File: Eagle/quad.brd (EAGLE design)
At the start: 72 x 46 mm, 12 parts

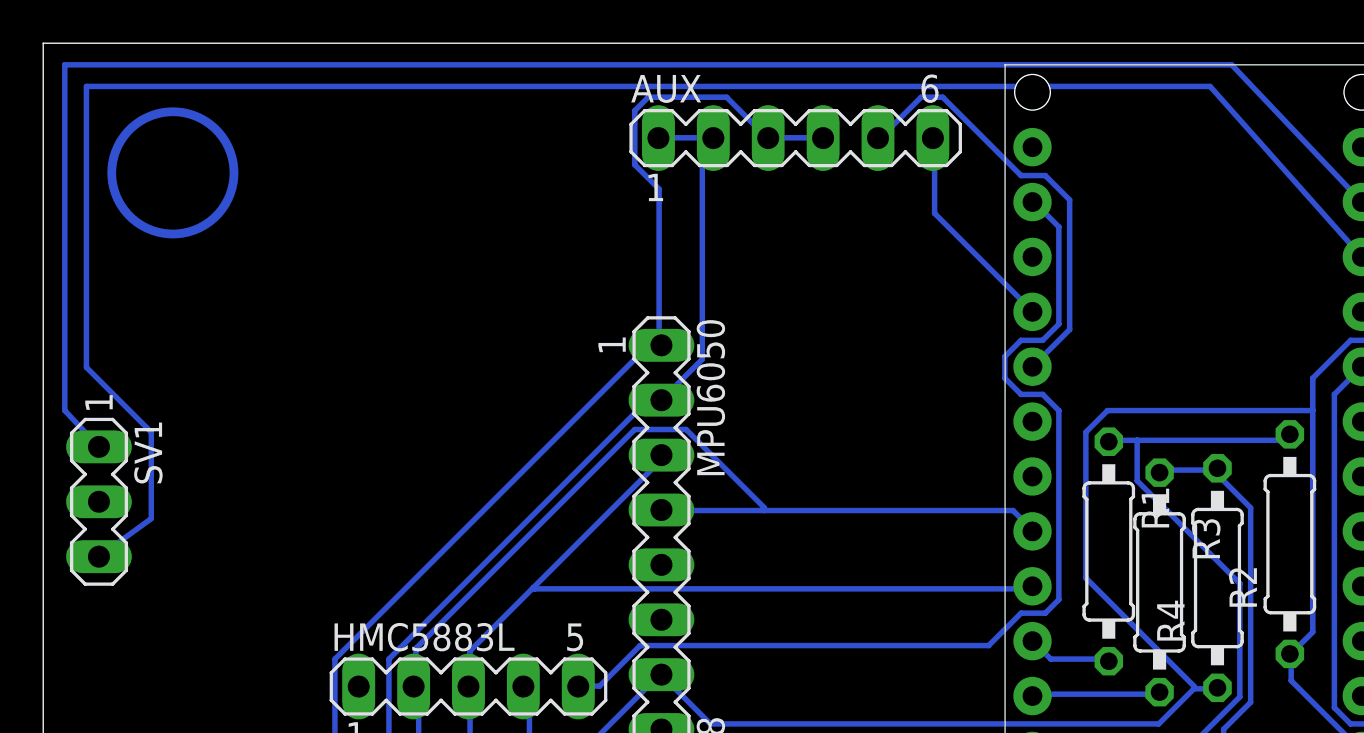
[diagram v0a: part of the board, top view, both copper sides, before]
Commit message: Added acrobtic mode. Not tested yet.
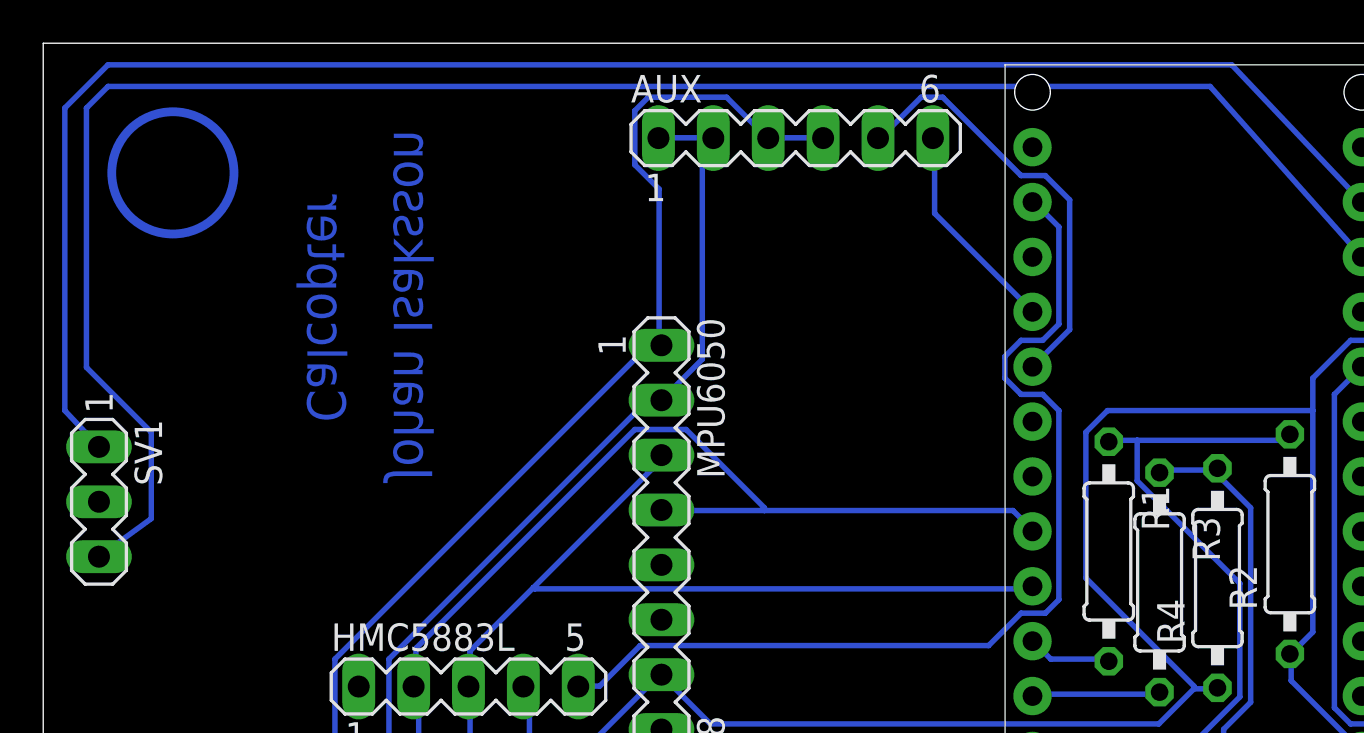
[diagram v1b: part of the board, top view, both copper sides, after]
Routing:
- net N$4: track 81.1 -> 79.9 mm
- net N$3: track 86.8 -> 86.2 mm
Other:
- board text added: "Calcopter"
- board text added: "Johan Isaksson"
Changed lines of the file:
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@@
 <?xml version="1.0" encoding="utf-8"?>
 <!DOCTYPE eagle SYSTEM "eagle.dtd">
-<eagle version="7.4.0">
+<eagle version="7.5.0">
 <drawing>
 <settings>
@@
 <layer number="17" name="Pads" color="2" fill="1" visible="yes" active="yes"/>
 <layer number="18" name="Vias" color="2" fill="1" visible="yes" active="yes"/>
-<layer number="19" name="Unrouted" color="6" fill="1" visible="yes" active="yes"/>
-<layer number="20" name="Dimension" color="15" fill="1" visible="yes" active="yes"/>
-<layer number="21" name="tPlace" color="7" fill="1" visible="yes" active="yes"/>
-<layer number="22" name="bPlace" color="7" fill="1" visible="yes" active="yes"/>
-<layer number="23" name="tOrigins" color="15" fill="1" visible="yes" active="yes"/>
-<layer number="24" name="bOrigins" color="15" fill="1" visible="yes" active="yes"/>
-<layer number="25" name="tNames" color="7" fill="1" visible="yes" active="yes"/>
-<layer number="26" name="bNames" color="7" fill="1" visible="yes" active="yes"/>
-<layer number="27" name="tValues" color="7" fill="1" visible="yes" active="yes"/>
-<layer number="28" name="bValues" color="7" fill="1" visible="yes" active="yes"/>
+<layer number="19" name="Unrouted" color="6" fill="1" visible="no" active="yes"/>
+<layer number="20" name="Dimension" color="15" fill="1" visible="no" active="yes"/>
+<layer number="21" name="tPlace" color="7" fill="1" visible="no" active="yes"/>
+<layer number="22" name="bPlace" color="7" fill="1" visible="no" active="yes"/>
+<layer number="23" name="tOrigins" color="15" fill="1" visible="no" active="yes"/>
+<layer number="24" name="bOrigins" color="15" fill="1" visible="no" active="yes"/>
+<layer number="25" name="tNames" color="7" fill="1" visible="no" active="yes"/>
+<layer number="26" name="bNames" color="7" fill="1" visible="no" active="yes"/>
+<layer number="27" name="tValues" color="7" fill="1" visible="no" active="yes"/>
+<layer number="28" name="bValues" color="7" fill="1" visible="no" active="yes"/>
 <layer number="29" name="tStop" color="7" fill="3" visible="no" active="yes"/>
 <layer number="30" name="bStop" color="7" fill="6" visible="no" active="yes"/>
@@
 <layer number="37" name="tTest" color="7" fill="1" visible="no" active="yes"/>
 <layer number="38" name="bTest" color="7" fill="1" visible="no" active="yes"/>
-<layer number="39" name="tKeepout" color="4" fill="11" visible="yes" active="yes"/>
-<layer number="40" name="bKeepout" color="1" fill="11" visible="yes" active="yes"/>
-<layer number="41" name="tRestrict" color="4" fill="10" visible="yes" active="yes"/>
-<layer number="42" name="bRestrict" color="1" fill="10" visible="yes" active="yes"/>
-<layer number="43" name="vRestrict" color="2" fill="10" visible="yes" active="yes"/>
+<layer number="39" name="tKeepout" color="4" fill="11" visible="no" active="yes"/>
+<layer number="40" name="bKeepout" color="1" fill="11" visible="no" active="yes"/>
+<layer number="41" name="tRestrict" color="4" fill="10" visible="no" active="yes"/>
+<layer number="42" name="bRestrict" color="1" fill="10" visible="no" active="yes"/>
+<layer number="43" name="vRestrict" color="2" fill="10" visible="no" active="yes"/>
 <layer number="44" name="Drills" color="7" fill="1" visible="no" active="yes"/>
 <layer number="45" name="Holes" color="7" fill="1" visible="no" active="yes"/>
 <layer number="46" name="Milling" color="3" fill="1" visible="no" active="yes"/>
 <layer number="47" name="Measures" color="7" fill="1" visible="no" active="yes"/>
-<layer number="48" name="Document" color="7" fill="1" visible="yes" active="yes"/>
-<layer number="49" name="Reference" color="7" fill="1" visible="yes" active="yes"/>
-<layer number="51" name="tDocu" color="7" fill="1" visible="yes" active="yes"/>
-<layer number="52" name="bDocu" color="7" fill="1" visible="yes" active="yes"/>
+<layer number="48" name="Document" color="7" fill="1" visible="no" active="yes"/>
+<layer number="49" name="Reference" color="7" fill="1" visible="no" active="yes"/>
+<layer number="51" name="tDocu" color="7" fill="1" visible="no" active="yes"/>
+<layer number="52" name="bDocu" color="7" fill="1" visible="no" active="yes"/>
 <layer number="90" name="Modules" color="5" fill="1" visible="no" active="no"/>
 <layer number="91" name="Nets" color="2" fill="1" visible="no" active="no"/>
@@
 <circle x="6" y="6" radius="2.828425" width="0.4064" layer="16"/>
 <circle x="66" y="6" radius="2.828425" width="0.4064" layer="16"/>
+<text x="18" y="42" size="1.778" layer="16" rot="MR270">Johan Isaksson</text>
+<text x="14" y="39" size="1.778" layer="16" rot="MR270">Calcopter</text>
 </plain>
 <attributes>
@@
 <wire x1="5" y1="24" x2="5" y2="28" width="0.254" layer="16"/>
 <wire x1="5" y1="28" x2="2" y2="31" width="0.254" layer="16"/>
-<wire x1="2" y1="31" x2="2" y2="44" width="0.254" layer="16"/>
-<wire x1="2" y1="44" x2="54" y2="44" width="0.254" layer="16"/>
+<wire x1="2" y1="44" x2="54" y2="44" width="0" layer="19" extent="1-16"/>
 <wire x1="54" y1="44" x2="61.02" y2="36.11" width="0.254" layer="16"/>
+<wire x1="2" y1="31" x2="2" y2="43" width="0.254" layer="16"/>
+<wire x1="2" y1="43" x2="3" y2="44" width="0.254" layer="16"/>
+<wire x1="3" y1="44" x2="54" y2="44" width="0.254" layer="16"/>
 </signal>
 <signal name="N$5">
@@
 <contactref element="SV1" pad="1"/>
 <wire x1="61.02" y1="38.65" x2="55" y2="45" width="0.254" layer="16"/>
-<wire x1="55" y1="45" x2="1" y2="45" width="0.254" layer="16"/>
-<wire x1="1" y1="45" x2="1" y2="29" width="0.254" layer="16"/>
 <wire x1="1" y1="29" x2="2.58" y2="27.32" width="0.254" layer="16"/>
+<wire x1="55" y1="45" x2="3" y2="45" width="0.254" layer="16"/>
+<wire x1="3" y1="45" x2="1" y2="43" width="0.254" layer="16"/>
+<wire x1="1" y1="43" x2="1" y2="29" width="0.254" layer="16"/>
 </signal>
 </signals>

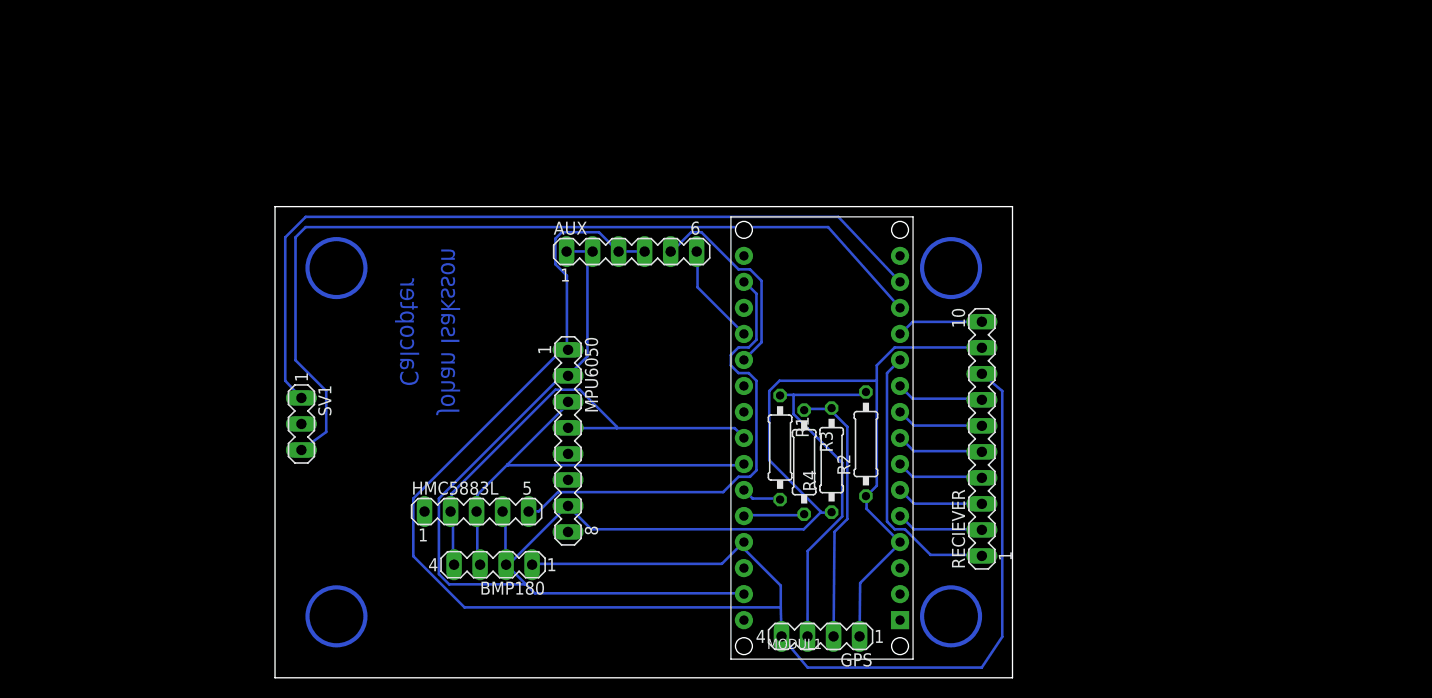
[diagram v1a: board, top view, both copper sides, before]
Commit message: Worked on board for the large quad.
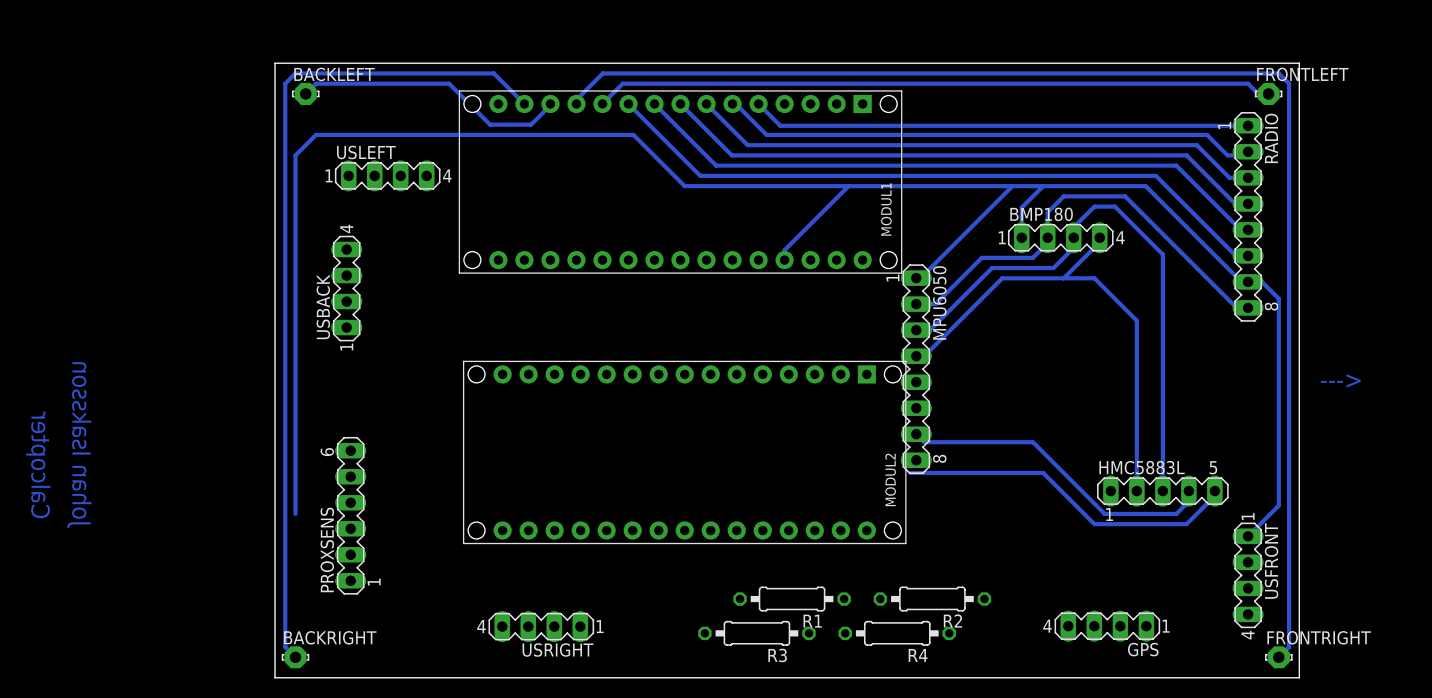
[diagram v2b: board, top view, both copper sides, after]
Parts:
- removed AUX: (no value), con-lstb:MA06-1
- removed RECIEVER: (no value), con-lstb:MA10-1
- removed SV1: (no value), con-lstb:MA03-1
- added BACKLEFT, BACKRIGHT, FRONTLEFT, FRONTRIGHT: LSP11, solpad:LSP11
- added MODUL2: ARDUINO_NANO2, arduino:ARDUINO_NANO2
- added PROXSENS: (no value), con-lstb:MA06-1
- added RADIO: (no value), con-lstb:MA08-1
- added USBACK, USFRONT, USLEFT, USRIGHT: (no value), con-lstb:MA04-1
- moved HMC5883L 67.0 mm to (86.7, 18.2)
- moved BMP180 64.0 mm to (76.7, 43.0), turned to 0 degrees
- moved MPU6050 34.7 mm to (62.6, 30.1)
- moved MODUL1 28.6 mm to (39.6, 48.4), turned to 270 degrees
- moved GPS 28.0 mm to (81.3, 5.04)
- moved R4 18.1 mm to (60.8, 4.34), turned to 180 degrees
- moved R3 17.3 mm to (47.0, 4.34), turned to 180 degrees
- moved R2 16.5 mm to (64.2, 7.69), turned to 180 degrees
- moved R1 14.8 mm to (50.5, 7.69), turned to 180 degrees
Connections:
- new net N$22: MODUL2.J1.7, USFRONT.2
- new net N$23: MODUL2.J1.8, USFRONT.3
- new net N$24: MODUL2.J1.5, USLEFT.2
- new net N$25: MODUL2.J1.6, USLEFT.3
- new net N$26: MODUL2.J1.9, USRIGHT.2
- new net N$27: MODUL2.J1.10, USRIGHT.3
- new net N$29: MODUL2.J1.12, USBACK.3
- new net N$30: MODUL2.J1.11, USBACK.2
- net AREF: now also MODUL2.J2.13
- net N$1: now also FRONTLEFT.MP; no longer RECIEVER.1
- net N$10: now also MODUL2.J2.11, PROXSENS.5; no longer AUX.6, MODUL1.J2.12
- net N$11: now also RADIO.4; no longer RECIEVER.5
- net N$12: now also RADIO.5; no longer RECIEVER.6
- net N$13: now also RADIO.6; no longer RECIEVER.7
- net N$14: now also MODUL2.J2.14
- net N$15: now also MODUL2.J2.5; no longer MODUL1.J2.5
- net N$16: now also MODUL2.J2.7
- net N$17: now also MODUL2.J2.8
- net N$18: now also MODUL2.J2.6; no longer MODUL1.J2.6
- net N$19: now also MODUL2.J2.12, PROXSENS.6; no longer AUX.5, MODUL1.J2.11
- net N$2: now also MODUL2.J2.4, PROXSENS.1, PROXSENS.2, RADIO.7, USBACK.1, USFRONT.1, USLEFT.1, USRIGHT.1; no longer AUX.3, AUX.4, RECIEVER.8
- net N$3: now also BACKLEFT.MP; no longer SV1.3
- net N$4: now also BACKRIGHT.MP; no longer SV1.1
- net N$5: now also RADIO.1; no longer RECIEVER.2
- net N$6: now also FRONTRIGHT.MP; no longer RECIEVER.10
- net N$7: now also RADIO.2; no longer RECIEVER.3
- net N$8: now also RADIO.3; no longer RECIEVER.4
- net N$9: now also MODUL2.J1.4, MODUL2.J2.2, PROXSENS.3, PROXSENS.4, RADIO.8, USBACK.4, USFRONT.4, USLEFT.4, USRIGHT.4; no longer AUX.1, AUX.2, RECIEVER.9
- net VIN: now also MODUL2.J2.1
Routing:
- net N$6: track 8.47 -> 127.9 mm
- net N$9: track 181.0 -> 74.5 mm
- net N$3: track 86.2 -> 26.9 mm
- net N$13: track 8.61 -> 66.6 mm
- net N$12: track 8.55 -> 63.0 mm
- net N$11: track 8.57 -> 59.4 mm
- net N$8: track 8.61 -> 55.9 mm
- net N$7: track 8.55 -> 52.6 mm
- net N$5: track 8.57 -> 48.7 mm
- net N$1: track 27.0 -> 66.3 mm
- net N$20: track 35.5 -> 0.00 mm
- net N$21: track 26.3 -> 0.00 mm
- net N$2: track 169.6 -> 191.7 mm
- net N$19: track 20.0 -> 0.00 mm
- net N$14: track 46.1 -> 33.4 mm
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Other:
- board size 72 x 46 mm -> 100 x 60 mm
- board text added: "<---"

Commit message: Simplified large board. Planning to put distance sensors on a separate board.
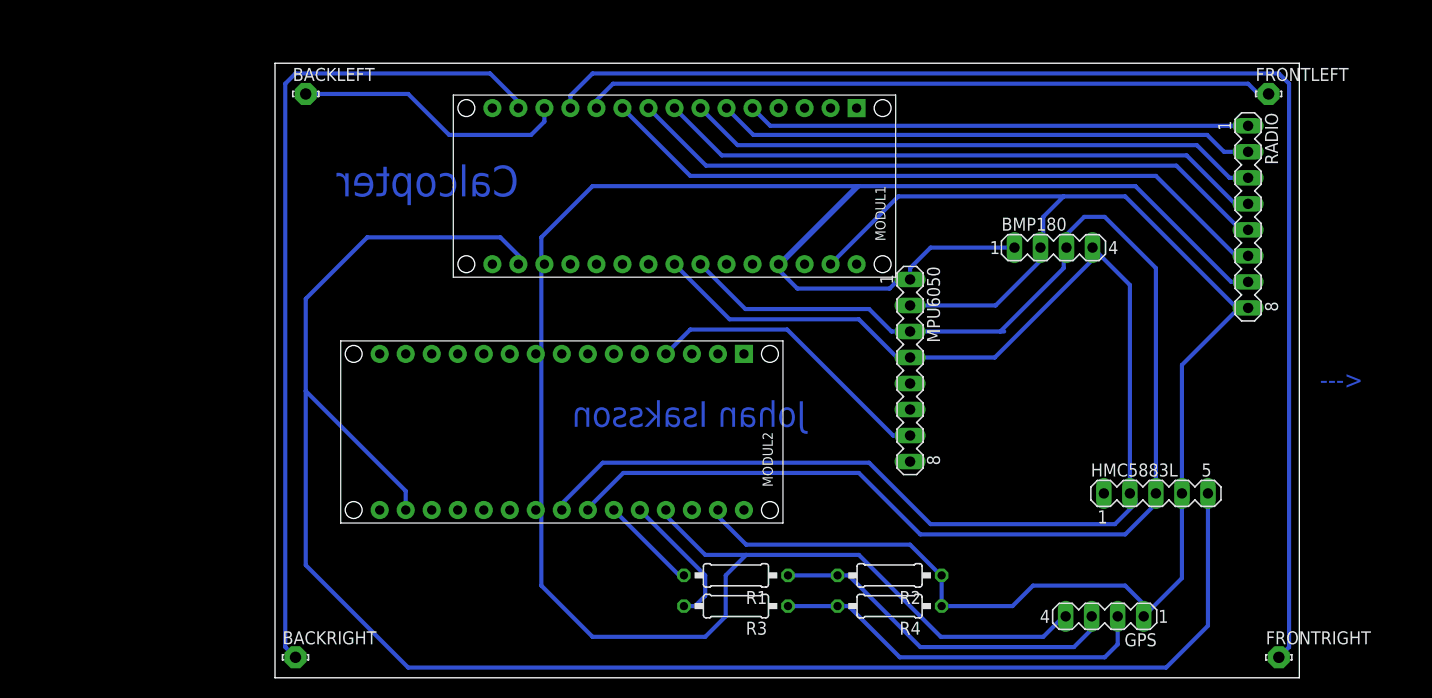
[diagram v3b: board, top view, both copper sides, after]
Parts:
- removed PROXSENS: (no value), con-lstb:MA06-1
- removed USBACK, USFRONT, USLEFT, USRIGHT: (no value), con-lstb:MA04-1
- moved MODUL2 12.2 mm to (28.0, 24.0)
- moved R1 5.95 mm to (45.0, 10.0)
- moved R2 4.78 mm to (60.0, 10.0)
- moved R3 3.36 mm to (45.0, 7.00)
- moved R4 2.76 mm to (60.0, 7.00)
- moved BMP180 1.19 mm to (76.0, 42.0)
- moved GPS 0.99 mm to (81.0, 6.00)
- moved HMC5883L 0.72 mm to (86.0, 18.0)
- moved MODUL1 0.71 mm to (39.0, 48.0)
- moved MPU6050 0.62 mm to (62.0, 30.0)
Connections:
- removed net N$10: MODUL2.J2.11, PROXSENS.5
- removed net N$19: MODUL2.J2.12, PROXSENS.6
- removed net N$22: MODUL2.J1.7, USFRONT.2
- removed net N$23: MODUL2.J1.8, USFRONT.3
- removed net N$24: MODUL2.J1.5, USLEFT.2
- removed net N$25: MODUL2.J1.6, USLEFT.3
- removed net N$26: MODUL2.J1.9, USRIGHT.2
- removed net N$27: MODUL2.J1.10, USRIGHT.3
- removed net N$29: MODUL2.J1.12, USBACK.3
- removed net N$30: MODUL2.J1.11, USBACK.2
- net N$2: no longer PROXSENS.1, PROXSENS.2, USBACK.1, USFRONT.1, USLEFT.1, USRIGHT.1
- net N$9: no longer PROXSENS.3, PROXSENS.4, USBACK.4, USFRONT.4, USLEFT.4, USRIGHT.4
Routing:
- net N$14: track 33.4 -> 173.5 mm
- net N$9: track 74.5 -> 184.5 mm
- net N$17: track 49.2 -> 138.2 mm
- net N$16: track 55.3 -> 139.9 mm
- net N$2: track 191.7 -> 231.0 mm
- net N$21: track 0.00 -> 37.5 mm
- net N$20: track 0.00 -> 34.5 mm
- net N$15: track 0.00 -> 13.5 mm
- net N$18: track 0.00 -> 9.48 mm
- net N$1: track 66.3 -> 67.8 mm
- net N$6: track 127.9 -> 129.1 mm
